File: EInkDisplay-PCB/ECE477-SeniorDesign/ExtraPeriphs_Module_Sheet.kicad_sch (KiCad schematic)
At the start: 0 parts

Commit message: fixing
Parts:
- added J1: SD_Card_Device, symbol Connector:SD_Card_Device
- added R2, R3, R4, R5, R6: 47k, symbol Device:R
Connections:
- new net: J1.7 (DAT0), R2.2
- new net: J1.8 (DAT1), R3.2
- new net: J1.1 (CD/DAT3), R5.2
- new net: J1.2 (CMD), R6.2
- new net: J1.9 (DAT2), R4.2
- new net +3.3V: J1.4 (VDD), R2.1, R3.1, R4.1, R5.1, R6.1
- new net GND: J1.3 (VSS), J1.6 (VSS)

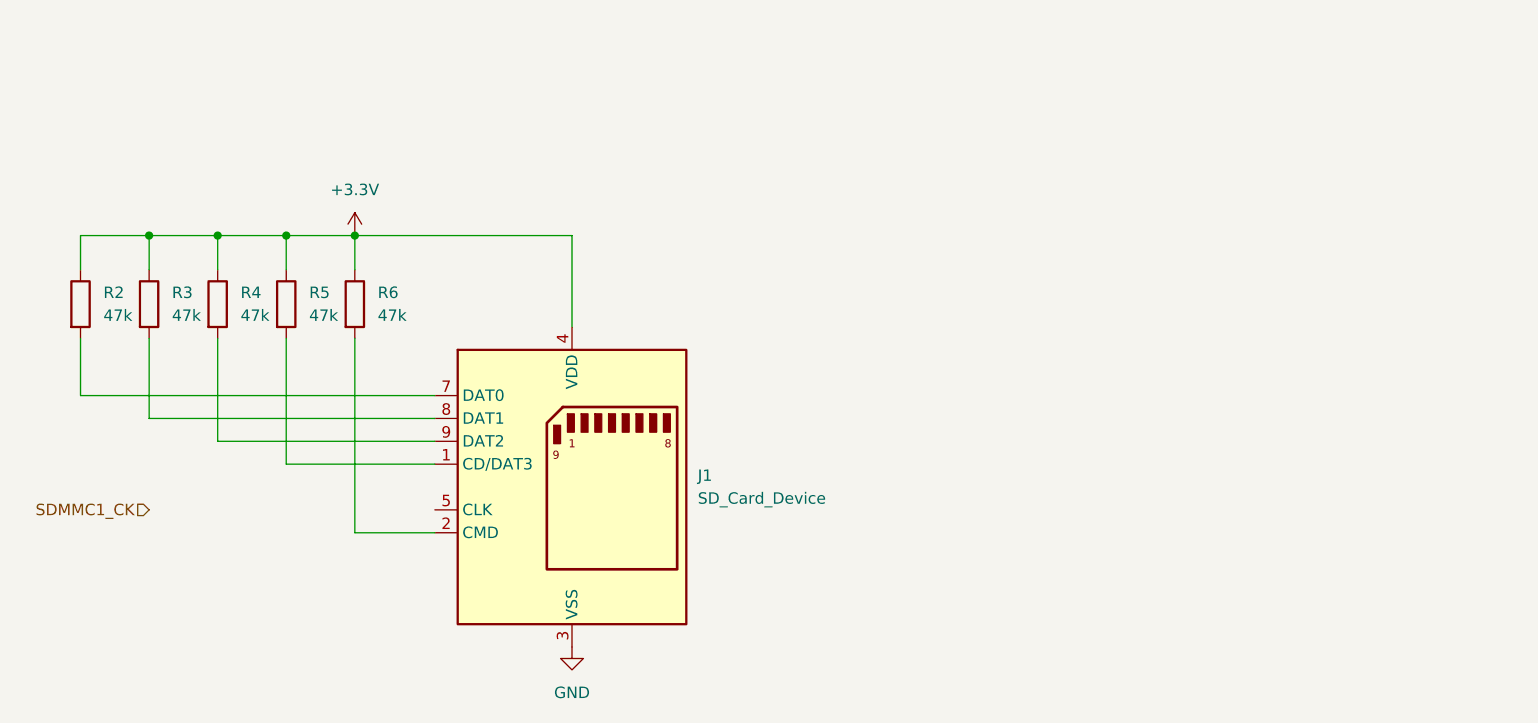
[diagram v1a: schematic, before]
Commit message: Fixing SD w SPI
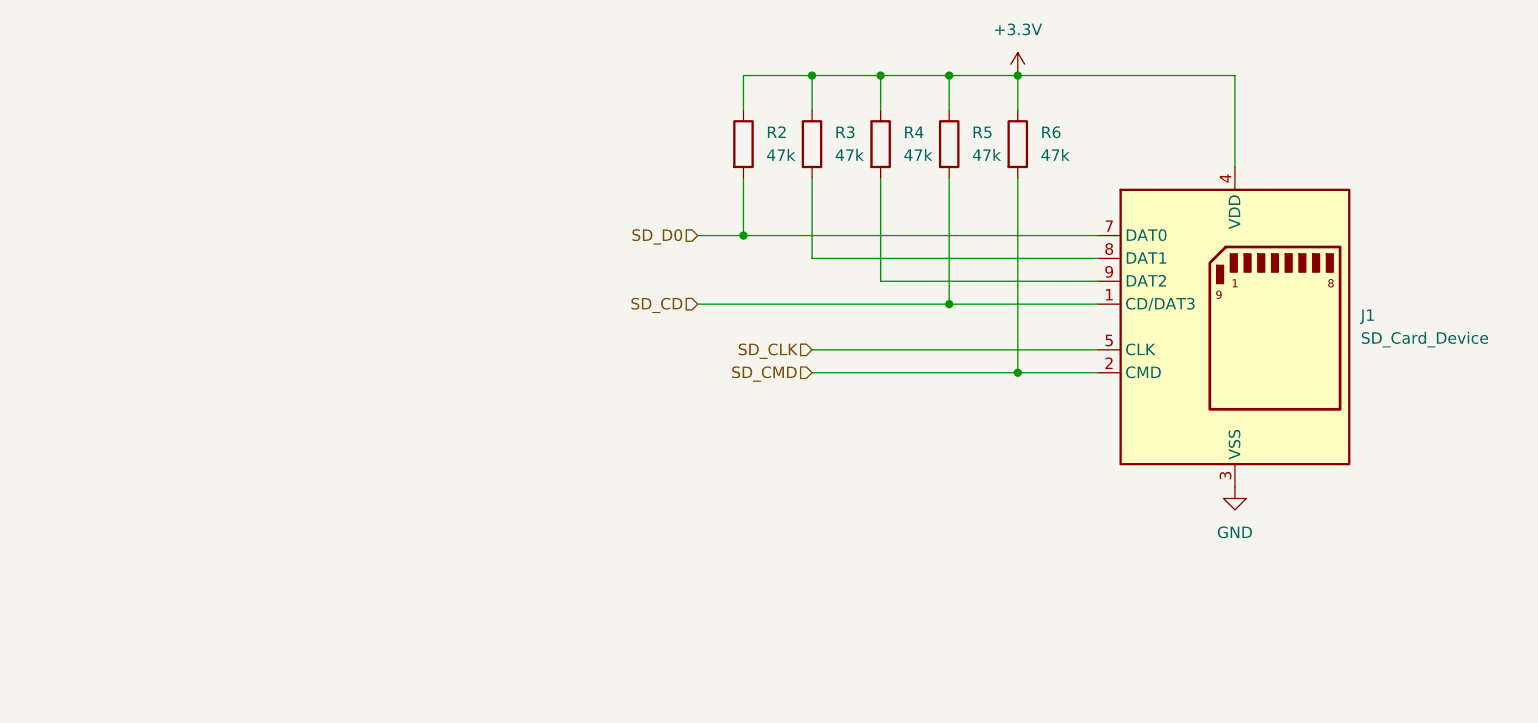
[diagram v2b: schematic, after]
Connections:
- net SD_D0: now reaches J1.7 (DAT0), R2.2
- net SD_CD: now reaches J1.1 (CD/DAT3), R5.2
- net SD_CMD: now reaches J1.2 (CMD), R6.2
- net SD_CLK: now reaches J1.5 (CLK)
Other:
- moved on the sheet: J1, R2, R3, R4, R5, R6

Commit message: push
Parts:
- added C21: 100nF, symbol Device:C_Small
- added C22, C24, C26: 10pF, symbol Device:C_Small
- added C23, C25, C27: 100n, symbol Device:C_Small
- added R10, R12, R14: 100k, symbol Device:R_Small
- added R11, R13, R15: 1k, symbol Device:R_Small
- added R7: 200, symbol Device:R_Small
- added R8, R9: 20k, symbol Device:R
- added SW2, SW3, SW4: SW_Push, symbol Switch:SW_Push
- R2, R3, R4, R5, R6: value 47k -> 20k
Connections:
- net +3.3V: now also J1.6 (VDD), C21.1, R8.1, R9.1, SW2.1, SW3.1, SW4.1; no longer J1.4 (VDD)
- net GND: now also J1.5 (VSS), C21.2, C22.2, C23.2, C24.2, C25.2, C26.2, C27.2, R10.2, R12.2, R14.2; no longer J1.3 (VSS), J1.6 (VSS)
- net SD_CD: now also R7.1; no longer J1.1 (CD/DAT3), R5.2
- net SD_CLK: now also J1.4 (CLK), R9.2; no longer J1.5 (CLK)
- net at J1.9 (CD), R4.2: now also R7.2
- net SD_CMD renamed SD_MOSI
- net SD_D0: no longer names the net of J1.7 (DAT1), R2.2
- new net: C24.1, R12.1, R13.1, SW3.2
- new net: C26.1, R14.1, R15.1, SW4.2
- new net: C22.1, R10.1, R11.1, SW2.2
- new net SD_CS: J1.1 (CS/DAT3), R5.2
- new net SD_MISO: J1.3 (MISO/DAT0), R8.2
- new net button1: C23.1, R11.2
- new net button2: C25.1, R13.2
- new net button3: C27.1, R15.2
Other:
- note added: "Push Buttons"
- note added: "SD CARD READER"
- moved on the sheet: R2, R3, R4, R5, R6

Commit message: Changes
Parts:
- removed SW2, SW3, SW4: SW_Push, symbol Switch:SW_Push
- added J3, J4, J5: JST Conn, symbol Connector_Generic:Conn_01x02
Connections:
- net +3.3V: now also J3.1 (Pin_1), J4.1 (Pin_1), J5.1 (Pin_1)
- net at C24.1, R12.1, R13.1: now also J4.2 (Pin_2)
- net at C26.1, R14.1, R15.1: now also J5.2 (Pin_2)
- net at C22.1, R10.1, R11.1: now also J3.2 (Pin_2)

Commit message: push
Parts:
- added TP1: SD_CD, symbol Connector:TestPoint
- added TP2: SD_CS, symbol Connector:TestPoint
- added TP3: SD_MOSI, symbol Connector:TestPoint
- added TP4: SD_MISO, symbol Connector:TestPoint
- added TP5: SD_CLK, symbol Connector:TestPoint
- C21: footprint (none) -> Capacitor_SMD:C_0603_1608Metric_Pad1.08x0.95mm_HandSolder
- R10, R11, R12, R13, R14, R15, R2, R3, R4, R5, R6, R7, R8, R9: footprint (none) -> Resistor_SMD:R_0603_1608Metric_Pad0.98x0.95mm_HandSolder
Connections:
- net SD_CLK: now also TP5.1
- net SD_CS: now also TP2.1
- net SD_MISO: now also TP4.1
- net SD_MOSI: now also TP3.1
- net at J1.9 (CD), R4.2, R7.2: now also TP1.1
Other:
- moved on the sheet: R2, R3, R4, R5, R6, R7, R9

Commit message: push
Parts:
- C21: footprint Capacitor_SMD:C_0603_1608Metric_Pad1.08x0.95mm_HandSolder -> Capacitor_SMD:C_0805_2012Metric_Pad1.18x1.45mm_HandSolder
- C22, C23, C24, C25, C26, C27: footprint (none) -> Capacitor_SMD:C_0805_2012Metric_Pad1.18x1.45mm_HandSolder
- J1: footprint (none) -> PCB_Lib:SD_Reader
- J3, J4, J5: footprint (none) -> PCB_Lib:JST Conn
- R10, R11, R12, R13, R14, R15, R2, R3, R4, R5, R6, R7, R8, R9: footprint Resistor_SMD:R_0603_1608Metric_Pad0.98x0.95mm_HandSolder -> Resistor_SMD:R_0805_2012Metric_Pad1.20x1.40mm_HandSolder
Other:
- note added: "reverse diodes"
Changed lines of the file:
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@@
+		)
+	)
+	(text "reverse diodes\n"
+		(exclude_from_sim no)
+		(at 32.004 102.616 0)
+		(effects
+			(font
+				(size 1.27 1.27)
+			)
 		)
 	)
@@
 			)
 		)
-		(property "Footprint" ""
+		(property "Footprint" "PCB_Lib:JST Conn"
 			(at 35.56 111.76 0)
 			(effects
@@
 			)
 		)
-		(property "Footprint" "Resistor_SMD:R_0603_1608Metric_Pad0.98x0.95mm_HandSolder"
+		(property "Footprint" "Resistor_SMD:R_0805_2012Metric_Pad1.20x1.40mm_HandSolder"
 			(at 31.242 29.21 90)
 			(effects
@@
 			)
 		)
-		(property "Footprint" "Resistor_SMD:R_0603_1608Metric_Pad0.98x0.95mm_HandSolder"
+		(property "Footprint" "Resistor_SMD:R_0805_2012Metric_Pad1.20x1.40mm_HandSolder"
 			(at 45.72 123.19 0)
 			(effects
@@
 			)
 		)
-		(property "Footprint" ""
+		(property "Footprint" "Capacitor_SMD:C_0805_2012Metric_Pad1.18x1.45mm_HandSolder"
 			(at 68.58 95.25 0)
 			(effects
@@
 			)
 		)
-		(property "Footprint" ""
+		(property "Footprint" "Capacitor_SMD:C_0805_2012Metric_Pad1.18x1.45mm_HandSolder"
 			(at 55.88 123.19 0)
 			(effects
@@
 			)
 		)
-		(property "Footprint" ""
+		(property "Footprint" "Capacitor_SMD:C_0805_2012Metric_Pad1.18x1.45mm_HandSolder"
 			(at 55.88 151.13 0)
 			(effects
@@
 			)
 		)
-		(property "Footprint" "Resistor_SMD:R_0603_1608Metric_Pad0.98x0.95mm_HandSolder"
+		(property "Footprint" "Resistor_SMD:R_0805_2012Metric_Pad1.20x1.40mm_HandSolder"
 			(at 79.502 29.21 90)
 			(effects
@@
 			)
 		)
-		(property "Footprint" ""
+		(property "Footprint" "Capacitor_SMD:C_0805_2012Metric_Pad1.18x1.45mm_HandSolder"
 			(at 68.58 151.13 0)
 			(effects
@@
 			)
 		)
-		(property "Footprint" "Resistor_SMD:R_0603_1608Metric_Pad0.98x0.95mm_HandSolder"
+		(property "Footprint" "Resistor_SMD:R_0805_2012Metric_Pad1.20x1.40mm_HandSolder"
 			(at 26.67 44.45 0)
 			(effects
@@
 			)
 		)
-		(property "Footprint" "Resistor_SMD:R_0603_1608Metric_Pad0.98x0.95mm_HandSolder"
+		(property "Footprint" "Resistor_SMD:R_0805_2012Metric_Pad1.20x1.40mm_HandSolder"
 			(at 45.72 151.13 0)
 			(effects
@@
 			)
 		)
-		(property "Footprint" ""
+		(property "Footprint" "PCB_Lib:JST Conn"
 			(at 35.56 139.7 0)
 			(effects
@@
 			)
 		)
-		(property "Footprint" "Resistor_SMD:R_0603_1608Metric_Pad0.98x0.95mm_HandSolder"
+		(property "Footprint" "Resistor_SMD:R_0805_2012Metric_Pad1.20x1.40mm_HandSolder"
 			(at 38.862 29.21 90)
 			(effects
@@
 			)
 		)
-		(property "Footprint" "Resistor_SMD:R_0603_1608Metric_Pad0.98x0.95mm_HandSolder"
+		(property "Footprint" "Resistor_SMD:R_0805_2012Metric_Pad1.20x1.40mm_HandSolder"
 			(at 46.482 29.21 90)
 			(effects
@@
 			)
 		)
-		(property "Footprint" "Resistor_SMD:R_0603_1608Metric_Pad0.98x0.95mm_HandSolder"
+		(property "Footprint" "Resistor_SMD:R_0805_2012Metric_Pad1.20x1.40mm_HandSolder"
 			(at 45.72 95.25 0)
 			(effects
@@
 			)
 		)
-		(property "Footprint" "Resistor_SMD:R_0603_1608Metric_Pad0.98x0.95mm_HandSolder"
+		(property "Footprint" "Resistor_SMD:R_0805_2012Metric_Pad1.20x1.40mm_HandSolder"
 			(at 63.5 116.84 0)
 			(effects
@@
 			)
 		)
-		(property "Footprint" ""
+		(property "Footprint" "PCB_Lib:JST Conn"
 			(at 35.56 83.82 0)
 			(effects
@@
 			)
 		)
-		(property "Footprint" "Resistor_SMD:R_0603_1608Metric_Pad0.98x0.95mm_HandSolder"
+		(property "Footprint" "Resistor_SMD:R_0805_2012Metric_Pad1.20x1.40mm_HandSolder"
 			(at 63.5 88.9 0)
 			(effects
@@
 			)
 		)
-		(property "Footprint" "Resistor_SMD:R_0603_1608Metric_Pad0.98x0.95mm_HandSolder"
+		(property "Footprint" "Resistor_SMD:R_0805_2012Metric_Pad1.20x1.40mm_HandSolder"
 			(at 61.722 29.21 90)
 			(effects
@@
 			)
 		)
-		(property "Footprint" "Resistor_SMD:R_0603_1608Metric_Pad0.98x0.95mm_HandSolder"
+		(property "Footprint" "Resistor_SMD:R_0805_2012Metric_Pad1.20x1.40mm_HandSolder"
 			(at 69.342 29.21 90)
 			(effects
@@
 			)
 		)
-		(property "Footprint" "Resistor_SMD:R_0603_1608Metric_Pad0.98x0.95mm_HandSolder"
+		(property "Footprint" "Resistor_SMD:R_0805_2012Metric_Pad1.20x1.40mm_HandSolder"
 			(at 63.5 144.78 0)
 			(effects
@@
 			)
 		)
-		(property "Footprint" ""
+		(property "Footprint" "Capacitor_SMD:C_0805_2012Metric_Pad1.18x1.45mm_HandSolder"
 			(at 55.88 95.25 0)
 			(effects
@@
 			)
 		)
-		(property "Footprint" "Capacitor_SMD:C_0603_1608Metric_Pad1.08x0.95mm_HandSolder"
+		(property "Footprint" "Capacitor_SMD:C_0805_2012Metric_Pad1.18x1.45mm_HandSolder"
 			(at 91.44 24.13 0)
 			(effects
@@
 			)
 		)
-		(property "Footprint" "Resistor_SMD:R_0603_1608Metric_Pad0.98x0.95mm_HandSolder"
+		(property "Footprint" "Resistor_SMD:R_0805_2012Metric_Pad1.20x1.40mm_HandSolder"
 			(at 54.102 29.21 90)
 			(effects
@@
 			)
 		)
-		(property "Footprint" ""
+		(property "Footprint" "Capacitor_SMD:C_0805_2012Metric_Pad1.18x1.45mm_HandSolder"
 			(at 68.58 123.19 0)
 			(effects
@@
 			)
 		)
-		(property "Footprint" ""
+		(property "Footprint" "PCB_Lib:SD_Reader"
 			(at 99.06 49.53 0)
 			(effects

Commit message: SD card updates
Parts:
- removed C21: 100nF, Capacitor_SMD:C_0805_2012Metric_Pad1.18x1.45mm_HandSolder, symbol Device:C_Small
- removed J1: SD_Card_Device, PCB_Lib:SD_Reader, symbol Connector:SD_Card_Device
- removed R2, R3, R4, R5, R6, R8, R9: 20k, Resistor_SMD:R_0805_2012Metric_Pad1.20x1.40mm_HandSolder, symbol Device:R
- removed R7: 200, Resistor_SMD:R_0805_2012Metric_Pad1.20x1.40mm_HandSolder, symbol Device:R_Small
- removed TP1: SD_CD, symbol Connector:TestPoint
- removed TP2: SD_CS, symbol Connector:TestPoint
- removed TP3: SD_MOSI, symbol Connector:TestPoint
- removed TP4: SD_MISO, symbol Connector:TestPoint
- removed TP5: SD_CLK, symbol Connector:TestPoint
- added C39: 100uF, symbol Device:C_Small
- added J9: Micro_SD_Card_Det1, PCB_Lib:SD_Reader, symbol Connector:Micro_SD_Card_Det1
- added R23: 121, symbol Device:R_Small
- added R24: 200, symbol Device:R_Small
- added R25, R26, R27, R28: 3.3k, symbol Device:R_Small
- added U8: LM1117DT-3.3, Package_TO_SOT_SMD:TO-252-3_TabPin2, symbol Regulator_Linear:LM1117DT-3.3
- added U9: 74LVC125APW_118, PCB_Lib:74LVC, symbol EinkComponentLibrary:74LVC125APW_118
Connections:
- net +3.3V: now also C39.1, J9.4 (VDD), R23.1, U8.2 (VO), U8.3 (VI), U9.14 (VCC)
- net GND: now also C39.2, J9.6 (VSS), R24.2, U8.1 (GND), U9.1 (*1OE), U9.10 (*3OE), U9.13 (*4OE), U9.4 (*2OE), U9.7 (GND)
- net SD_CS: now also R28.2
- net SD_MISO: now also U9.11 (4Y)
- net SD_MOSI: now also R25.1
- new net: R26.2, U9.5 (2A)
- new net: R25.2, U9.2 (1A)
- new net: R27.1, U9.12 (4A)
- new net: R28.1, U9.9 (3A)
- new net: R23.2, R24.1
- new net CS_LLC: U9.8 (3Y)
- new net CS_LLS: J9.2 (DAT3/CD)
- new net DI_LLS: J9.3 (CMD), U9.3 (1Y)
- new net DO_LLC: R27.2
- new net DO_LLS: J9.7 (DAT0)
- new net SCK_LLS: J9.5 (CLK), U9.6 (2Y)
- new net SD_SCK: R26.1
- no-connect marks 0 -> 4
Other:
- moved on the sheet: C22, C23, C24, C25, C26, C27, J3, J4, J5, R10, R11, R12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

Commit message: changes
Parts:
- removed C39: 100uF, symbol Device:C_Small
- removed R23: 121, symbol Device:R_Small
- removed R24: 200, symbol Device:R_Small
- removed U8: LM1117DT-3.3, Package_TO_SOT_SMD:TO-252-3_TabPin2, symbol Regulator_Linear:LM1117DT-3.3
- added D1, D2, D3: D, symbol Device:D
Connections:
- net at J4.2 (Pin_2), R12.1: now also D2.2 (A); no longer C24.1, R13.1
- net at C26.1, R15.1: now also D3.1 (K); no longer J5.2 (Pin_2), R14.1
- net at C22.1, R11.1: now also D1.1 (K); no longer J3.2 (Pin_2), R10.1
- new net: D3.2 (A), J5.2 (Pin_2), R14.1
- new net: C24.1, D2.1 (K), R13.1
- new net: D1.2 (A), J3.2 (Pin_2), R10.1
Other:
- note removed: "reverse diodes"
- moved on the sheet: J9
